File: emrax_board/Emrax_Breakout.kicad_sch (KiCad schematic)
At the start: 3 parts, among them J1 Conn_01x09, J2 Conn_01x09

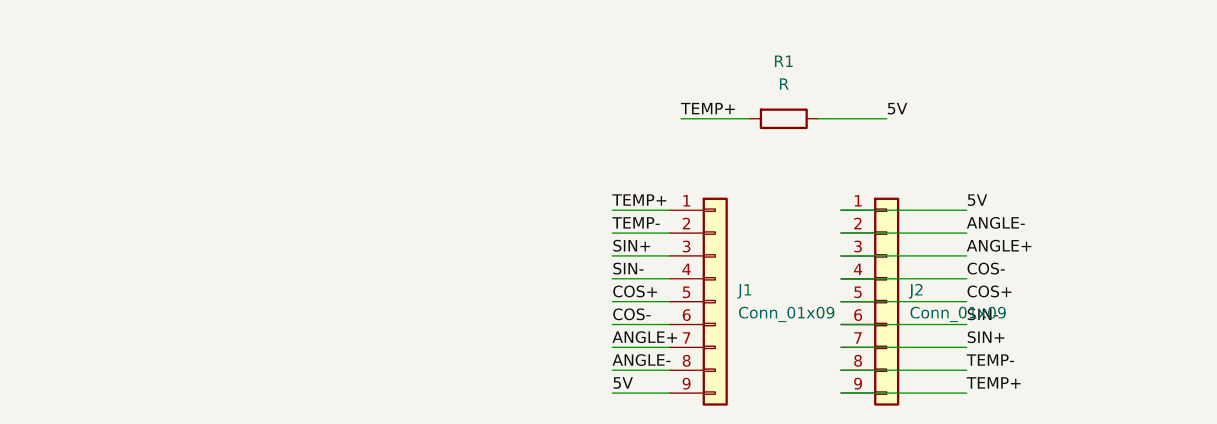
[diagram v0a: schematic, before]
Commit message: updating emrax breakout board
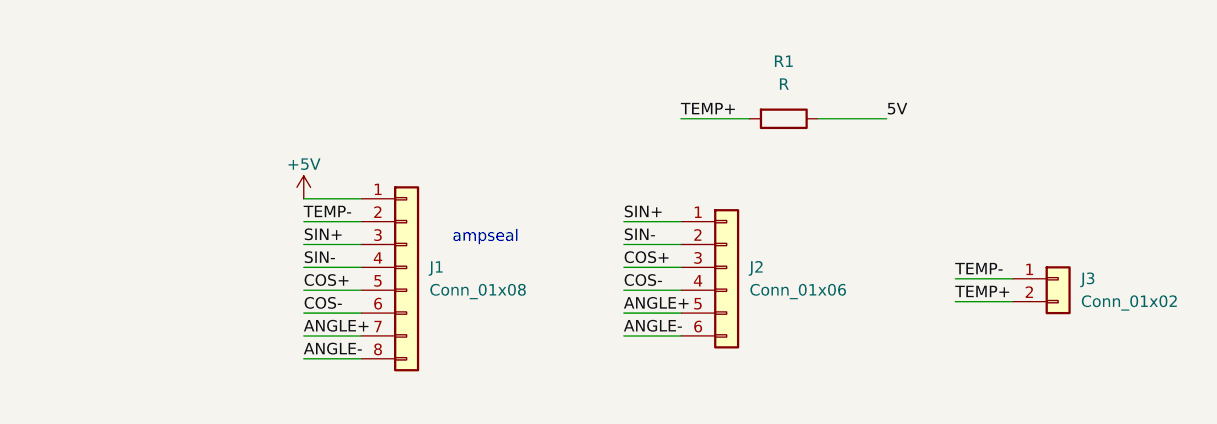
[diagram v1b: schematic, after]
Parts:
- removed J1, J2: Conn_01x09, Connector_JST:JST_XH_S9B-XH-A-1_1x09_P2.50mm_Horizontal, symbol Connector_Generic:Conn_01x09
- added J1: Conn_01x08, Connector_JST:JST_XH_B8B-XH-A_1x08_P2.50mm_Vertical, symbol Connector_Generic:Conn_01x08
- added J2: Conn_01x06, Connector_JST:JST_XH_S6B-XH-A-1_1x06_P2.50mm_Horizontal, symbol Connector_Generic:Conn_01x06
- added J3: Conn_01x02, Connector_JST:JST_XH_S2B-XH-A-1_1x02_P2.50mm_Horizontal, symbol Connector_Generic:Conn_01x02
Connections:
- net ANGLE+: now also J1.7 (Pin_7), J2.5 (Pin_5)
- net ANGLE-: now also J1.8 (Pin_8), J2.6 (Pin_6)
- net COS+: now also J1.5 (Pin_5), J2.3 (Pin_3)
- net COS-: now also J1.6 (Pin_6), J2.4 (Pin_4)
- net SIN+: now also J1.3 (Pin_3), J2.1 (Pin_1)
- net SIN-: now also J1.4 (Pin_4), J2.2 (Pin_2)
- net TEMP+: now also J3.2 (Pin_2)
- net TEMP-: now also J1.2 (Pin_2), J3.1 (Pin_1)
- new net +5V: J1.1 (Pin_1)
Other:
- note added: "ampseal"

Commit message: change schem and finish layout Ready for Review
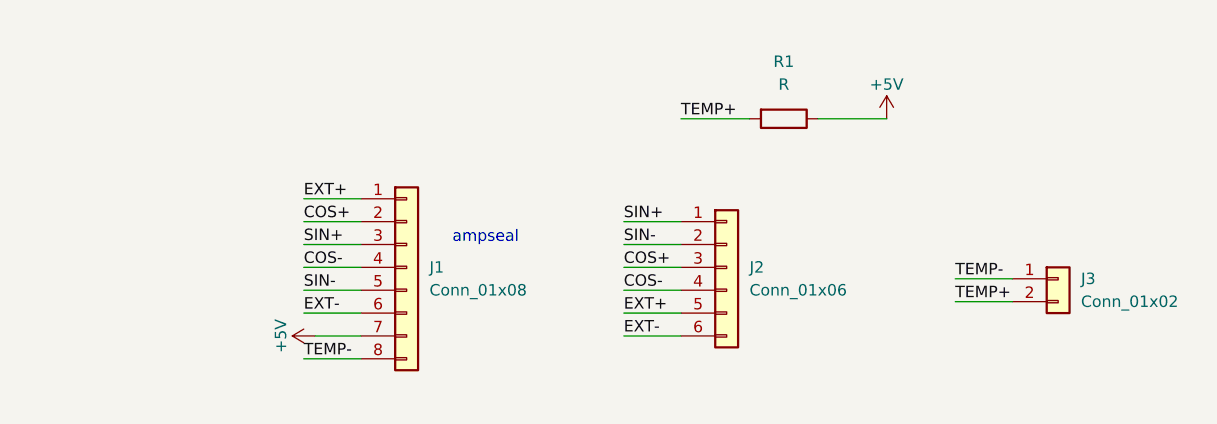
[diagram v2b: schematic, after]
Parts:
- J1: footprint Connector_JST:JST_XH_B8B-XH-A_1x08_P2.50mm_Vertical -> AERO_Footprints:TE_1-776280-1_8pin_Horizontal
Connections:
- net 5V is gone; now on net +5V: R1.1
- net +5V: now also J1.7 (Pin_7); no longer J1.1 (Pin_1)
- net COS+: now also J1.2 (Pin_2); no longer J1.5 (Pin_5)
- net COS-: now also J1.4 (Pin_4); no longer J1.6 (Pin_6)
- net SIN-: now also J1.5 (Pin_5); no longer J1.4 (Pin_4)
- net TEMP-: now also J1.8 (Pin_8); no longer J1.2 (Pin_2)
- net ANGLE+ renamed EXT+
- net EXT+: now also J1.1 (Pin_1); no longer J1.7 (Pin_7)
- net ANGLE- renamed EXT-
- net EXT-: now also J1.6 (Pin_6); no longer J1.8 (Pin_8)
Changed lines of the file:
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@@
 (kicad_sch (version 20211123) (generator eeschema)
   (paper "A4")
-  (wire (pts (xy 80.01 77.47) (xy 86.36 77.47))
-    (stroke (width 0) (type default) (color 0 0 0 0))
-  )
   (wire (pts (xy 80.01 62.23) (xy 86.36 62.23))
     (stroke (width 0) (type default) (color 0 0 0 0))
   )
+  (wire (pts (xy 81.28 77.47) (xy 86.36 77.47))
+    (stroke (width 0) (type default) (color 0 0 0 0))
+  )
   (wire (pts (xy 115.57 72.39) (xy 121.92 72.39))
     (stroke (width 0) (type default) (color 0 0 0 0))
@@
     (stroke (width 0) (type default) (color 0 0 0 0))
   )
+  (wire (pts (xy 80.01 80.01) (xy 86.36 80.01))
+    (stroke (width 0) (type default) (color 0 0 0 0))
+  )
+  (wire (pts (xy 80.01 74.93) (xy 86.36 74.93))
+    (stroke (width 0) (type default) (color 0 0 0 0))
+  )
+  (wire (pts (xy 137.16 53.34) (xy 144.78 53.34))
+    (stroke (width 0) (type default) (color 0 0 0 0))
+  )
   (wire (pts (xy 80.01 64.77) (xy 86.36 64.77))
     (stroke (width 0) (type default) (color 0 0 0 0))
   )
-  (wire (pts (xy 137.16 53.34) (xy 144.78 53.34))
+  (wire (pts (xy 152.4 71.12) (xy 158.75 71.12))
+    (stroke (width 0) (type default) (color 0 0 0 0))
+  )
+  (wire (pts (xy 80.01 69.85) (xy 86.36 69.85))
+    (stroke (width 0) (type default) (color 0 0 0 0))
+  )
+  (wire (pts (xy 115.57 67.31) (xy 121.92 67.31))
+    (stroke (width 0) (type default) (color 0 0 0 0))
+  )
+  (wire (pts (xy 115.57 69.85) (xy 121.92 69.85))
+    (stroke (width 0) (type default) (color 0 0 0 0))
+  )
+  (wire (pts (xy 152.4 73.66) (xy 158.75 73.66))
+    (stroke (width 0) (type default) (color 0 0 0 0))
+  )
+  (wire (pts (xy 80.01 67.31) (xy 86.36 67.31))
+    (stroke (width 0) (type default) (color 0 0 0 0))
+  )
+  (wire (pts (xy 115.57 77.47) (xy 121.92 77.47))
+    (stroke (width 0) (type default) (color 0 0 0 0))
+  )
+  (wire (pts (xy 115.57 64.77) (xy 121.92 64.77))
     (stroke (width 0) (type default) (color 0 0 0 0))
   )
@@
     (stroke (width 0) (type default) (color 0 0 0 0))
   )
-  (wire (pts (xy 80.01 80.01) (xy 86.36 80.01))
-    (stroke (width 0) (type default) (color 0 0 0 0))
-  )
-  (wire (pts (xy 152.4 71.12) (xy 158.75 71.12))
-    (stroke (width 0) (type default) (color 0 0 0 0))
-  )
-  (wire (pts (xy 80.01 74.93) (xy 86.36 74.93))
-    (stroke (width 0) (type default) (color 0 0 0 0))
-  )
-  (wire (pts (xy 115.57 67.31) (xy 121.92 67.31))
-    (stroke (width 0) (type default) (color 0 0 0 0))
-  )
-  (wire (pts (xy 115.57 69.85) (xy 121.92 69.85))
-    (stroke (width 0) (type default) (color 0 0 0 0))
-  )
-  (wire (pts (xy 152.4 73.66) (xy 158.75 73.66))
-    (stroke (width 0) (type default) (color 0 0 0 0))
-  )
-  (wire (pts (xy 80.01 67.31) (xy 86.36 67.31))
-    (stroke (width 0) (type default) (color 0 0 0 0))
-  )
-  (wire (pts (xy 115.57 77.47) (xy 121.92 77.47))
-    (stroke (width 0) (type default) (color 0 0 0 0))
-  )
-  (wire (pts (xy 115.57 64.77) (xy 121.92 64.77))
-    (stroke (width 0) (type default) (color 0 0 0 0))
-  )
-  (wire (pts (xy 80.01 69.85) (xy 86.36 69.85))
-    (stroke (width 0) (type default) (color 0 0 0 0))
-  )
   (text "ampseal\n" (at 96.52 67.31 0)
     (effects (font (size 1.27 1.27)) (justify left bottom))
@@
     (effects (font (size 1.27 1.27)) (justify left bottom))
   )
-  (label "COS-" (at 80.01 74.93 0)
+  (label "COS-" (at 80.01 69.85 0)
     (effects (font (size 1.27 1.27)) (justify left bottom))
   )
@@
     (effects (font (size 1.27 1.27)) (justify left bottom))
   )
+  (label "EXT+" (at 80.01 62.23 0)
+    (effects (font (size 1.27 1.27)) (justify left bottom))
+  )
   (label "TEMP+" (at 152.4 73.66 0)
     (effects (font (size 1.27 1.27)) (justify left bottom))
@@
     (effects (font (size 1.27 1.27)) (justify left bottom))
   )
-  (label "TEMP-" (at 80.01 64.77 0)
-    (effects (font (size 1.27 1.27)) (justify left bottom))
-  )
-  (label "5V" (at 144.78 53.34 0)
-    (effects (font (size 1.27 1.27)) (justify left bottom))
-  )
-  (label "ANGLE-" (at 115.57 77.47 0)
+  (label "TEMP-" (at 80.01 80.01 0)
+    (effects (font (size 1.27 1.27)) (justify left bottom))
+  )
+  (label "EXT-" (at 115.57 77.47 0)
     (effects (font (size 1.27 1.27)) (justify left bottom))
   )
@@
     (effects (font (size 1.27 1.27)) (justify left bottom))
   )
-  (label "ANGLE+" (at 115.57 74.93 0)
-    (effects (font (size 1.27 1.27)) (justify left bottom))
-  )
-  (label "COS+" (at 80.01 72.39 0)
+  (label "EXT+" (at 115.57 74.93 0)
+    (effects (font (size 1.27 1.27)) (justify left bottom))
+  )
+  (label "COS+" (at 80.01 64.77 0)
     (effects (font (size 1.27 1.27)) (justify left bottom))
   )
@@
     (effects (font (size 1.27 1.27)) (justify left bottom))
   )
-  (label "ANGLE-" (at 80.01 80.01 0)
-    (effects (font (size 1.27 1.27)) (justify left bottom))
-  )
-  (label "ANGLE+" (at 80.01 77.47 0)
-    (effects (font (size 1.27 1.27)) (justify left bottom))
-  )
-  (label "SIN-" (at 80.01 69.85 0)
+  (label "EXT-" (at 80.01 74.93 0)
+    (effects (font (size 1.27 1.27)) (justify left bottom))
+  )
+  (label "SIN-" (at 80.01 72.39 0)
     (effects (font (size 1.27 1.27)) (justify left bottom))
   )
@@
     (effects (font (size 1.27 1.27)) (justify left bottom))
   )
-  (symbol (lib_id "power:+5V") (at 80.01 62.23 0) (unit 1)
+  (symbol (lib_id "power:+5V") (at 81.28 77.47 90) (unit 1)
     (in_bom yes) (on_board yes)
-    (property "Reference" "#PWR0101" (id 0) (at 80.01 66.04 0)
-      (effects (font (size 1.27 1.27)) hide)
-    )
-    (property "Value" "+5V" (id 1) (at 80.01 58.42 0))
-    (property "Footprint" "" (id 2) (at 80.01 62.23 0)
-      (effects (font (size 1.27 1.27)) hide)
-    )
-    (property "Datasheet" "" (id 3) (at 80.01 62.23 0)
+    (property "Reference" "#PWR0101" (id 0) (at 85.09 77.47 0)
+      (effects (font (size 1.27 1.27)) hide)
+    )
+    (property "Value" "+5V" (id 1) (at 77.47 77.47 0))
+    (property "Footprint" "" (id 2) (at 81.28 77.47 0)
+      (effects (font (size 1.27 1.27)) hide)
+    )
+    (property "Datasheet" "" (id 3) (at 81.28 77.47 0)
       (effects (font (size 1.27 1.27)) hide)
     )
@@
     (pin "2")
   )
+  (symbol (lib_id "power:+5V") (at 144.78 53.34 0) (unit 1)
+    (in_bom yes) (on_board yes)
+    (property "Reference" "#PWR0102" (id 0) (at 144.78 57.15 0)
+      (effects (font (size 1.27 1.27)) hide)
+    )
+    (property "Value" "+5V" (id 1) (at 144.78 49.53 0))
+    (property "Footprint" "" (id 2) (at 144.78 53.34 0)
+      (effects (font (size 1.27 1.27)) hide)
+    )
+    (property "Datasheet" "" (id 3) (at 144.78 53.34 0)
+      (effects (font (size 1.27 1.27)) hide)
+    )
+    (pin "1")
+  )
   (symbol (lib_id "Connector_Generic:Conn_01x08") (at 91.44 69.85 0) (unit 1)
     (in_bom yes) (on_board yes) (fields_autoplaced)
@@
       (effects (font (size 1.27 1.27)) (justify left))
     )
-    (property "Footprint" "Connector_JST:JST_XH_B8B-XH-A_1x08_P2.50mm_Vertical" (id 2) (at 91.44 69.85 0)
+    (property "Footprint" "AERO_Footprints:TE_1-776280-1_8pin_Horizontal" (id 2) (at 91.44 69.85 0)
       (effects (font (size 1.27 1.27)) hide)
     )
@@
       (reference "#PWR0101") (unit 1) (value "+5V") (footprint "")
     )
+    (path "/c3ca3a76-d595-4d87-96fa-b1ba84644057"
+      (reference "#PWR0102") (unit 1) (value "+5V") (footprint "")
+    )
     (path "/ee86ad28-2e8a-4b4f-a90f-b244d52f0462"
-      (reference "J1") (unit 1) (value "Conn_01x08") (footprint "Connector_JST:JST_XH_B8B-XH-A_1x08_P2.50mm_Vertical")
+      (reference "J1") (unit 1) (value "Conn_01x08") (footprint "AERO_Footprints:TE_1-776280-1_8pin_Horizontal")
     )
     (path "/6a6ecbfc-48aa-4ae4-9206-987546f0d066"

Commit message: Addded comments
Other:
- note added: "10k Pull up"
- note added: "From Rinehart Analog 5v Pin"
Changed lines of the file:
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@@
     (stroke (width 0) (type default) (color 0 0 0 0))
+  )
+  (text "From Rinehart Analog 5v Pin" (at 48.26 71.755 0)
+    (effects (font (size 1.27 1.27) (thickness 0.254) bold italic) (justify left bottom))
+  )
+  (text "10k Pull up\n" (at 128.27 44.45 0)
+    (effects (font (size 1.27 1.27) bold italic) (justify left bottom))
   )
   (text "ampseal\n" (at 96.52 67.31 0)
